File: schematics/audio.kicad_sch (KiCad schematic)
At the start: 63 parts, among them J18 SPEAKER, J19 PHONEJACK, J5 Left Audio, J6 Right Audio, Q1 2n3904, U12 EN5503DOC, U17 41464, U18 41464, U19 41464, U20 41464

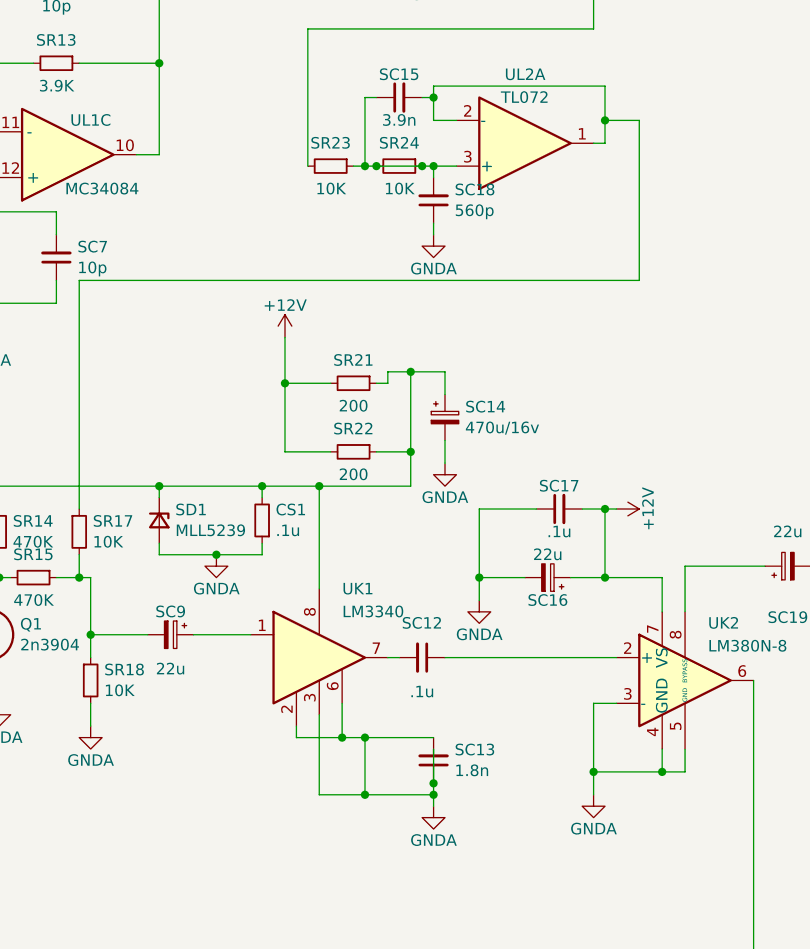
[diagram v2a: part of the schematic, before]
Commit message: Added a lot of missing footprints in the audio-section. Adjusted the PCB layout and re-routed the board.
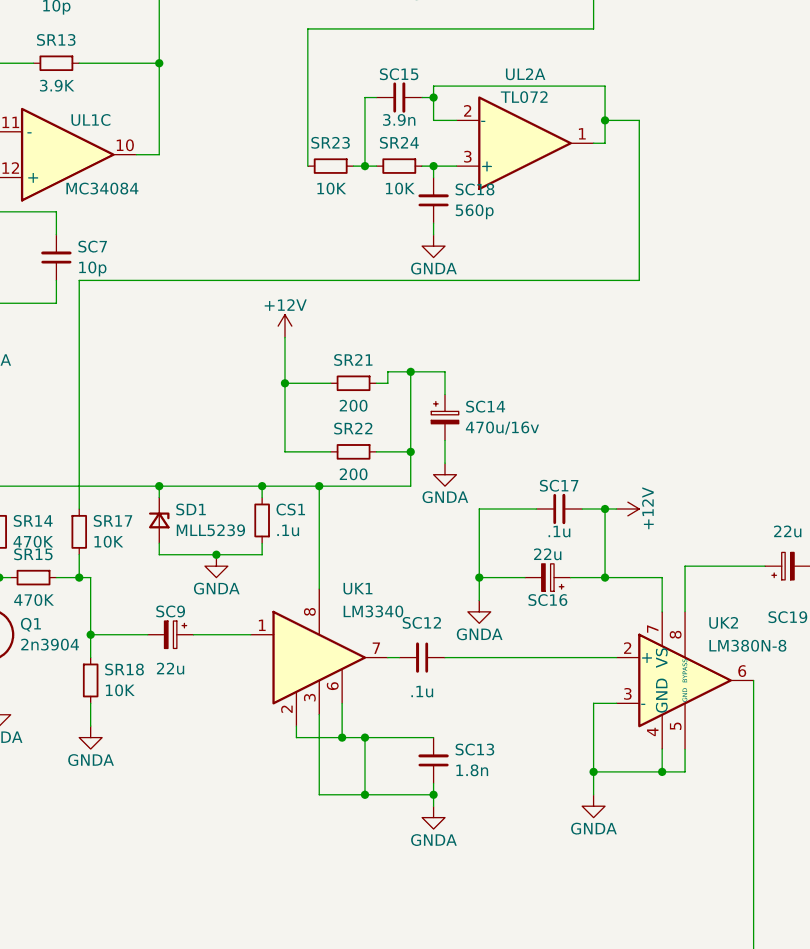
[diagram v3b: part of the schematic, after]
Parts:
- C17, SC1, SC10, SC11, SC12, SC13, SC14, SC15, SC16, SC17, SC18, SC19, SC2, SC3, SC4, SC5, SC6, SC7, SC8, SC9: footprint (none) -> Capacitor_THT:CP_Radial_D4.0mm_P1.50mm
- CS1, SR1, SR10, SR11, SR12, SR13, SR14, SR15, SR16, SR17, SR18, SR19, SR2, SR20, SR21, SR22, SR23, SR24, SR3, SR4, SR5, SR6, SR7, SR8, SR9: footprint (none) -> Resistor_SMD:R_0805_2012Metric_Pad1.20x1.40mm_HandSolder
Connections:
- net at SC18.2, SR24.1, UL2.3 (+): no longer SC15.1, SR23.1, SR24.2
- new net: SC15.1, SR23.1, SR24.2
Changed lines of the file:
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@@
 	)
 	(junction
-		(at 229.87 57.15)
-		(diameter 0)
-		(color 0 0 0 0)
-	)
-	(junction
 		(at 143.51 134.62)
 		(diameter 0)
@@
 	)
 	(junction
-		(at 236.22 125.73)
-		(diameter 0)
-		(color 0 0 0 0)
-	)
-	(junction
-		(at 234.95 57.15)
-		(diameter 0)
-		(color 0 0 0 0)
-	)
-	(junction
 		(at 175.26 39.37)
 		(diameter 0)
@@
 	(wire
 		(pts
-			(xy 229.87 57.15) (xy 234.95 57.15)
-		)
-		(stroke
-			(width 0)
-			(type default)
-		)
-	)
-	(wire
-		(pts
 			(xy 114.3 116.84) (xy 123.19 116.84)
 		)
@@
 	(wire
 		(pts
-			(xy 236.22 121.92) (xy 236.22 125.73)
-		)
-		(stroke
-			(width 0)
-			(type default)
-		)
-	)
-	(wire
-		(pts
 			(xy 175.26 76.2) (xy 176.53 76.2)
 		)
@@
 			)
 		)
-		(property "Footprint" ""
+		(property "Footprint" "Resistor_SMD:R_0805_2012Metric_Pad1.20x1.40mm_HandSolder"
 			(at 52.07 172.72 0)
 			(effects
@@
 			)
 		)
-		(property "Footprint" ""
+		(property "Footprint" "Capacitor_THT:CP_Radial_D4.0mm_P1.50mm"
 			(at 232.41 19.05 0)
 			(effects
@@
 			)
 		)
-		(property "Footprint" ""
+		(property "Footprint" "Resistor_SMD:R_0805_2012Metric_Pad1.20x1.40mm_HandSolder"
 			(at 165.1 59.69 0)
 			(effects
@@
 			)
 		)
-		(property "Footprint" ""
+		(property "Footprint" "Capacitor_THT:CP_Radial_D4.0mm_P1.50mm"
 			(at 237.49 85.09 0)
 			(effects
@@
 			)
 		)
-		(property "Footprint" ""
+		(property "Footprint" "Capacitor_THT:CP_Radial_D4.0mm_P1.50mm"
 			(at 38.1 166.37 0)
 			(effects
@@
 			)
 		)
-		(property "Footprint" ""
+		(property "Footprint" "Capacitor_THT:CP_Radial_D4.0mm_P1.50mm"
 			(at 194.31 36.83 0)
 			(effects
@@
 			)
 		)
-		(property "Footprint" ""
+		(property "Footprint" "Resistor_SMD:R_0805_2012Metric_Pad1.20x1.40mm_HandSolder"
 			(at 232.41 57.15 0)
 			(effects
@@
 			)
 		)
-		(property "Footprint" ""
+		(property "Footprint" "Resistor_SMD:R_0805_2012Metric_Pad1.20x1.40mm_HandSolder"
 			(at 227.33 88.9 0)
 			(effects
@@
 			)
 		)
-		(property "Footprint" ""
+		(property "Footprint" "Resistor_SMD:R_0805_2012Metric_Pad1.20x1.40mm_HandSolder"
 			(at 38.1 157.48 0)
 			(effects
@@
 			)
 		)
-		(property "Footprint" ""
+		(property "Footprint" "Capacitor_THT:CP_Radial_D4.0mm_P1.50mm"
 			(at 163.83 31.75 0)
 			(effects
@@
 			)
 		)
-		(property "Footprint" ""
+		(property "Footprint" "Capacitor_THT:CP_Radial_D4.0mm_P1.50mm"
 			(at 34.29 179.07 0)
 			(effects
@@
 			)
 		)
-		(property "Footprint" ""
+		(property "Footprint" "Capacitor_THT:CP_Radial_D4.0mm_P1.50mm"
 			(at 275.59 101.6 0)
 			(effects
@@
 			)
 		)
-		(property "Footprint" ""
+		(property "Footprint" "Resistor_SMD:R_0805_2012Metric_Pad1.20x1.40mm_HandSolder"
 			(at 224.79 57.15 0)
 			(effects
@@
 			)
 		)
-		(property "Footprint" ""
+		(property "Footprint" "Capacitor_THT:CP_Radial_D4.0mm_P1.50mm"
 			(at 236.22 123.19 0)
 			(effects
@@
 			)
 		)
-		(property "Footprint" ""
+		(property "Footprint" "Resistor_SMD:R_0805_2012Metric_Pad1.20x1.40mm_HandSolder"
 			(at 232.41 26.67 0)
 			(effects
@@
 			)
 		)
-		(property "Footprint" ""
+		(property "Footprint" "Capacitor_THT:CP_Radial_D4.0mm_P1.50mm"
 			(at 236.22 60.96 0)
 			(effects
@@
 			)
 		)
-		(property "Footprint" ""
+		(property "Footprint" "Capacitor_THT:CP_Radial_D4.0mm_P1.50mm"
 			(at 250.19 95.25 0)
 			(effects
@@
 			)
 		)
-		(property "Footprint" ""
+		(property "Footprint" "Resistor_SMD:R_0805_2012Metric_Pad1.20x1.40mm_HandSolder"
 			(at 217.17 96.52 0)
 			(effects
@@
 			)
 		)
-		(property "Footprint" ""
+		(property "Footprint" "Resistor_SMD:R_0805_2012Metric_Pad1.20x1.40mm_HandSolder"
 			(at 176.53 109.22 0)
 			(effects
@@
 			)
 		)
-		(property "Footprint" ""
+		(property "Footprint" "Resistor_SMD:R_0805_2012Metric_Pad1.20x1.40mm_HandSolder"
 			(at 194.31 45.72 0)
 			(effects
@@
 			)
 		)
-		(property "Footprint" ""
+		(property "Footprint" "Capacitor_THT:CP_Radial_D4.0mm_P1.50mm"
 			(at 232.41 49.53 0)
 			(effects
@@
 			)
 		)
-		(property "Footprint" ""
+		(property "Footprint" "Resistor_SMD:R_0805_2012Metric_Pad1.20x1.40mm_HandSolder"
 			(at 198.12 114.3 0)
 			(effects
@@
 			)
 		)
-		(property "Footprint" ""
+		(property "Footprint" "Resistor_SMD:R_0805_2012Metric_Pad1.20x1.40mm_HandSolder"
 			(at 223.52 19.05 0)
 			(effects
@@
 			)
 		)
-		(property "Footprint" ""
+		(property "Footprint" "Capacitor_THT:CP_Radial_D4.0mm_P1.50mm"
 			(at 165.1 67.31 0)
 			(effects
@@
 			)
 		)
-		(property "Footprint" ""
+		(property "Footprint" "Capacitor_THT:CP_Radial_D4.0mm_P1.50mm"
 			(at 114.3 124.46 0)
 			(effects
@@
 			)
 		)
-		(property "Footprint" ""
+		(property "Footprint" "Resistor_SMD:R_0805_2012Metric_Pad1.20x1.40mm_HandSolder"
 			(at 186.69 67.31 0)
 			(effects
@@
 			)
 		)
-		(property "Footprint" ""
+		(property "Footprint" "Capacitor_THT:CP_Radial_D4.0mm_P1.50mm"
 			(at 207.01 109.22 0)
 			(effects
@@
 			)
 		)
-		(property "Footprint" ""
+		(property "Footprint" "Resistor_SMD:R_0805_2012Metric_Pad1.20x1.40mm_HandSolder"
 			(at 45.72 166.37 0)
 			(effects
@@
 			)
 		)
-		(property "Footprint" ""
+		(property "Footprint" "Resistor_SMD:R_0805_2012Metric_Pad1.20x1.40mm_HandSolder"
 			(at 196.85 97.79 0)
 			(effects
@@
 			)
 		)
-		(property "Footprint" ""
+		(property "Footprint" "Capacitor_THT:CP_Radial_D4.0mm_P1.50mm"
 			(at 74.93 173.99 0)
 			(effects
@@
 			)
 		)
-		(property "Footprint" ""
+		(property "Footprint" "Resistor_SMD:R_0805_2012Metric_Pad1.20x1.40mm_HandSolder"
 			(at 27.94 165.1 0)
 			(effects
@@
 			)
 		)
-		(property "Footprint" ""
+		(property "Footprint" "Resistor_SMD:R_0805_2012Metric_Pad1.20x1.40mm_HandSolder"
 			(at 191.77 102.87 0)
 			(effects
@@
 			)
 		)
-		(property "Footprint" ""
+		(property "Footprint" "Resistor_SMD:R_0805_2012Metric_Pad1.20x1.40mm_HandSolder"
 			(at 179.07 53.34 0)
 			(effects
@@
 			)
 		)
-		(property "Footprint" ""
+		(property "Footprint" "Capacitor_THT:CP_Radial_D4.0mm_P1.50mm"
 			(at 234.95 111.76 0)
 			(effects
@@
 			)
 		)
-		(property "Footprint" ""
+		(property "Footprint" "Resistor_SMD:R_0805_2012Metric_Pad1.20x1.40mm_HandSolder"
 			(at 34.29 173.99 0)
 			(effects
@@
 			)
 		)
-		(property "Footprint" ""
+		(property "Footprint" "Capacitor_THT:CP_Radial_D4.0mm_P1.50mm"
 			(at 215.9 26.67 0)
 			(effects
@@
 			)
 		)
-		(property "Footprint" ""
+		(property "Footprint" "Resistor_SMD:R_0805_2012Metric_Pad1.20x1.40mm_HandSolder"
 			(at 147.32 134.62 0)
 			(effects
@@
 			)
 		)
-		(property "Footprint" ""
+		(property "Footprint" "Capacitor_THT:CP_Radial_D4.0mm_P1.50mm"
 			(at 236.22 30.48 0)
 			(effects
@@
 			)
 		)
-		(property "Footprint" ""
+		(property "Footprint" "Resistor_SMD:R_0805_2012Metric_Pad1.20x1.40mm_HandSolder"
 			(at 180.34 58.42 0)
 			(effects
@@
 			)
 		)
-		(property "Footprint" ""
+		(property "Footprint" "Resistor_SMD:R_0805_2012Metric_Pad1.20x1.40mm_HandSolder"
 			(at 163.83 39.37 0)
 			(effects
@@
 			)
 		)
-		(property "Footprint" ""
+		(property "Footprint" "Resistor_SMD:R_0805_2012Metric_Pad1.20x1.40mm_HandSolder"
 			(at 187.96 97.79 0)
 			(effects
@@
 			)
 		)
-		(property "Footprint" ""
+		(property "Footprint" "Resistor_SMD:R_0805_2012Metric_Pad1.20x1.40mm_HandSolder"
 			(at 227.33 81.28 0)
 			(effects
@@
 			)
 		)
-		(property "Footprint" ""
+		(property "Footprint" "Resistor_SMD:R_0805_2012Metric_Pad1.20x1.40mm_HandSolder"
 			(at 210.82 19.05 0)
 			(effects
@@
 			)
 		)
-		(property "Footprint" ""
+		(property "Footprint" "Capacitor_THT:CP_Radial_D4.0mm_P1.50mm"
 			(at 248.92 102.87 0)
 			(effects
@@
 			)
 		)
-		(property "Footprint" ""
+		(property "Footprint" "Capacitor_THT:CP_Radial_D4.0mm_P1.50mm"
 			(at 194.31 67.31 0)
 			(effects

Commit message: Added the rest of the footprints for the analog audio and re-did the layout and routing of the PCB.
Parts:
- UK1: footprint (none) -> Package_TO_SOT_SMD:SOT-23
- UL1: footprint (none) -> Package_DIP:DIP-8_W7.62mm_Socket
- UL2: footprint (none) -> Package_TO_SOT_SMD:SOT-23-5
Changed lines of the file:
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@@
 			)
 		)
-		(property "Footprint" ""
+		(property "Footprint" "Package_DIP:DIP-8_W7.62mm_Socket"
 			(at 195.58 55.88 0)
 			(effects
@@
 			)
 		)
-		(property "Footprint" ""
+		(property "Footprint" "Package_TO_SOT_SMD:SOT-23"
 			(at 223.52 111.76 0)
 			(effects
@@
 			)
 		)
-		(property "Footprint" ""
+		(property "Footprint" "Package_DIP:DIP-8_W7.62mm_Socket"
 			(at 130.81 119.38 0)
 			(effects
@@
 			)
 		)
-		(property "Footprint" ""
+		(property "Footprint" "Package_TO_SOT_SMD:SOT-23-5"
 			(at 245.11 21.59 0)
 			(effects
@@
 			)
 		)
-		(property "Footprint" ""
+		(property "Footprint" "Package_DIP:DIP-8_W7.62mm_Socket"
 			(at 167.64 48.26 0)
 			(effects
@@
 			)
 		)
-		(property "Footprint" ""
+		(property "Footprint" "Package_TO_SOT_SMD:SOT-23-5"
 			(at 246.38 54.61 0)
 			(effects
@@
 			)
 		)
-		(property "Footprint" ""
+		(property "Footprint" "Package_DIP:DIP-8_W7.62mm_Socket"
 			(at 167.64 76.2 0)
 			(effects
